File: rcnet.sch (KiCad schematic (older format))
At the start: 32 parts

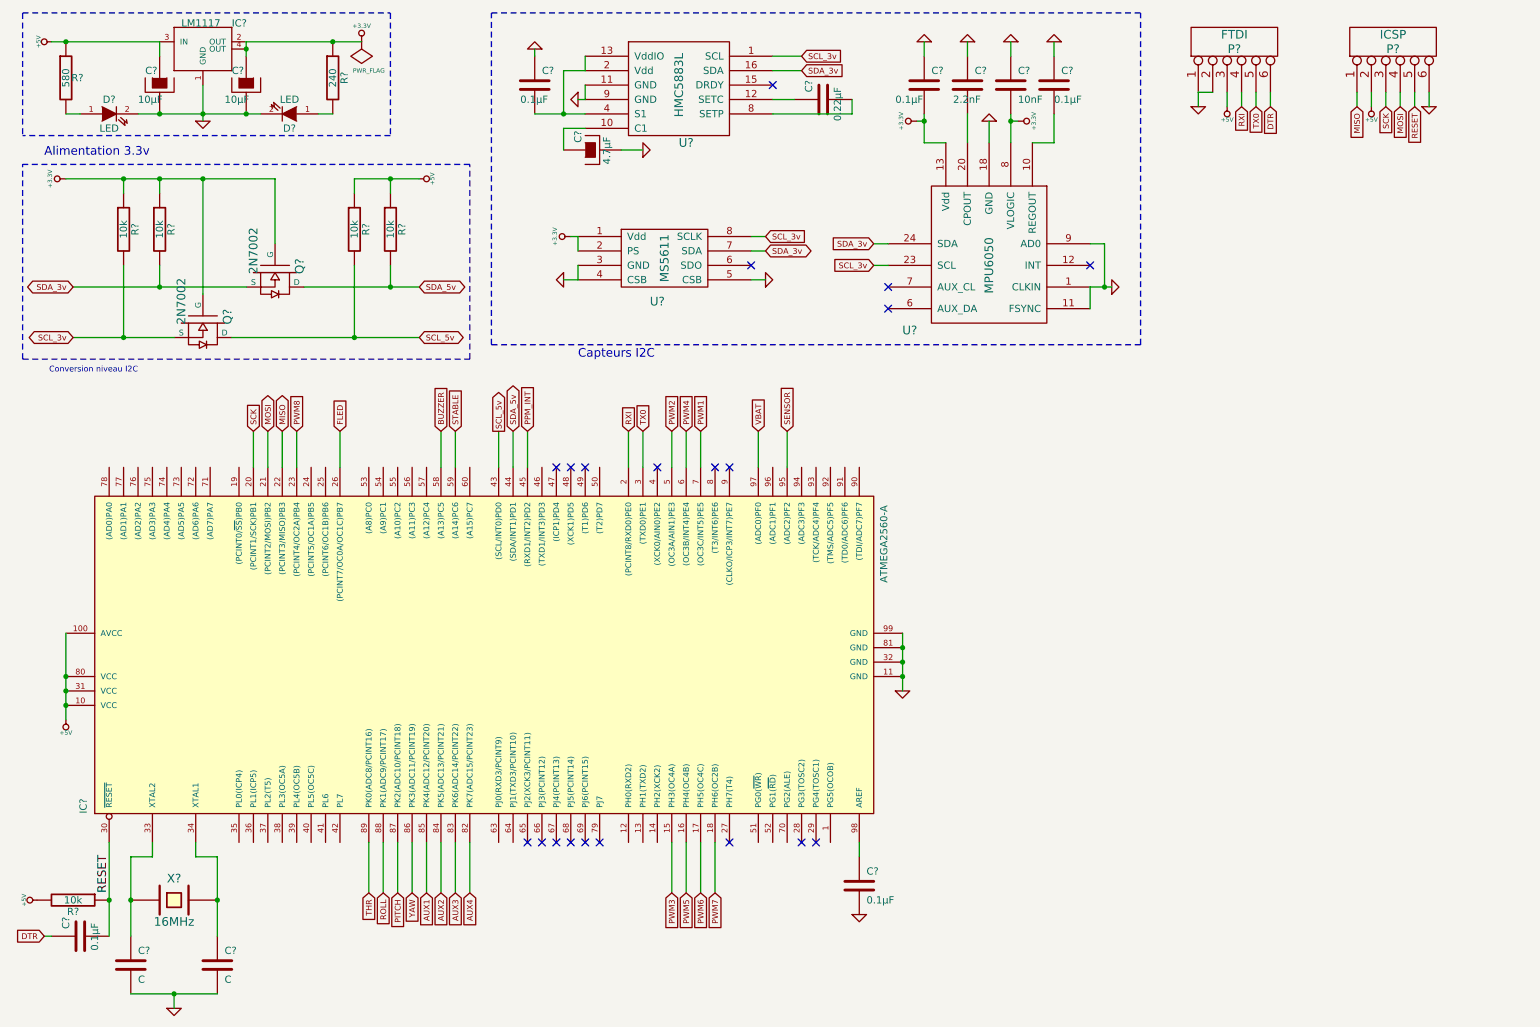
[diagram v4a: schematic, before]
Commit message: Cablage des I/O terminé, test ERC passé
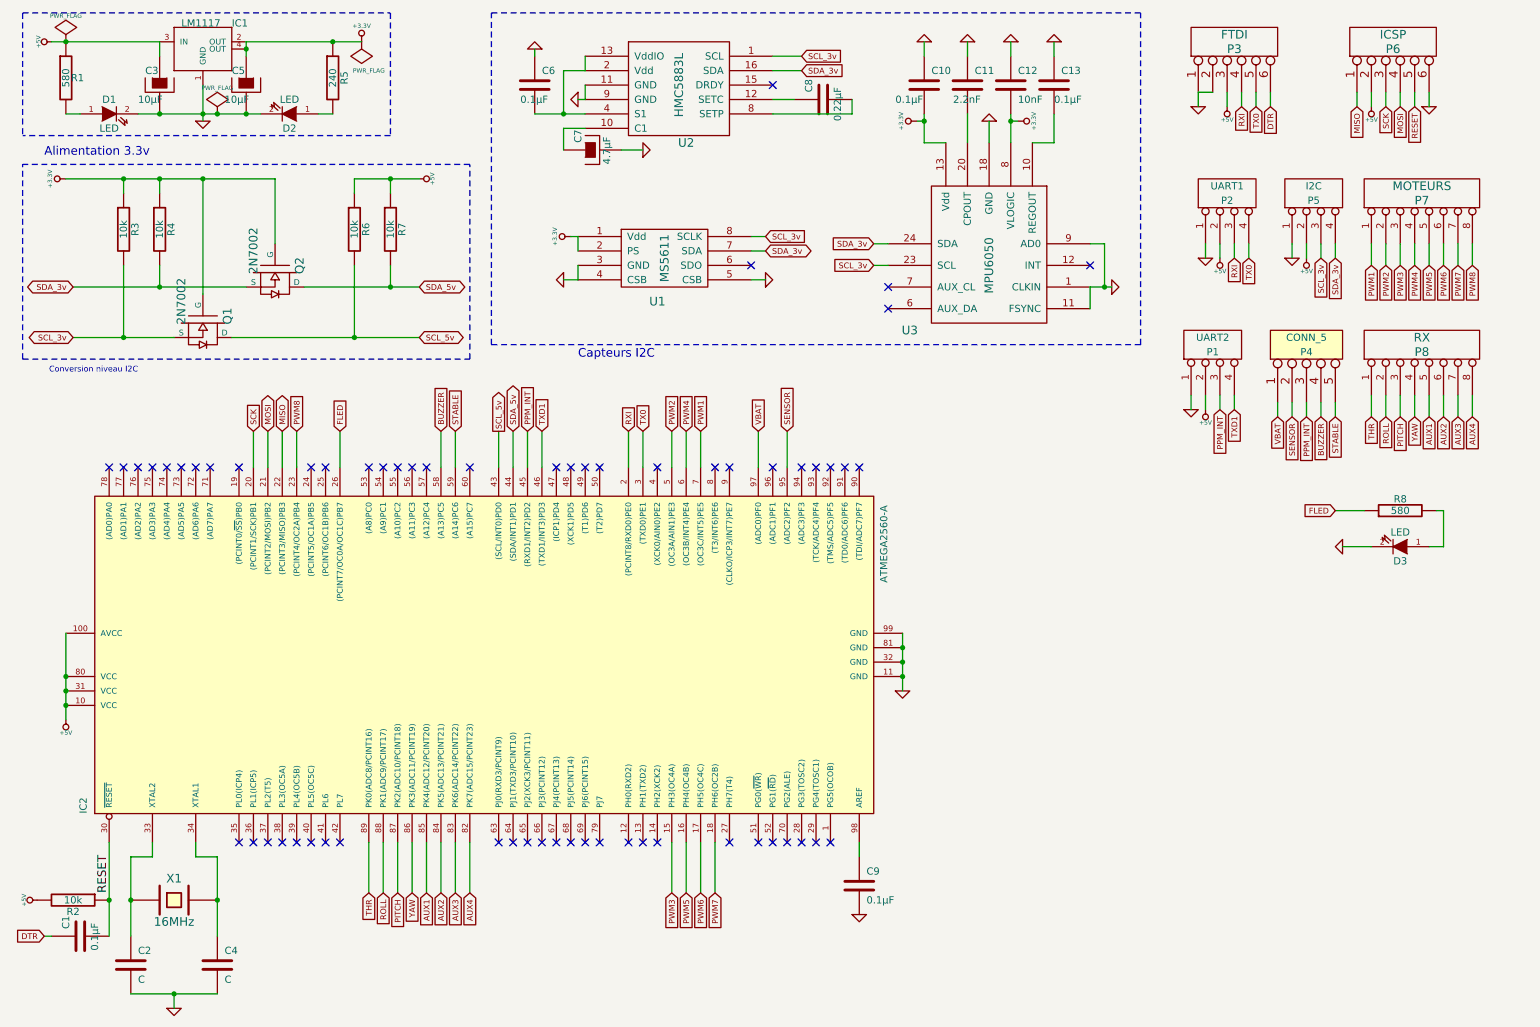
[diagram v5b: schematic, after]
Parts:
- added D3: LED, symbol LED
- added P1: UART2, symbol CONN_4
- added P2: UART1, symbol CONN_4
- added P4: CONN_5, symbol CONN_5
- added P5: I2C, symbol CONN_4
- added P7: MOTEURS, symbol CONN_8
- added P8: RX, symbol CONN_8
- added R8: 580, symbol R
- gave numbers to parts that had none: 32
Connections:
- net +5V: now also P1.2 (P2), P2.2 (P2), P5.2 (P2)
- net AUX1: now also P8.5 (P5)
- net AUX2: now also P8.6 (P6)
- net AUX3: now also P8.7 (P7)
- net AUX4: now also P8.8 (P8)
- net BUZZER: now also P4.4
- net FLED: now also R8.1
- net GND: now also D3.2 (K), P1.1 (P1), P2.1 (P1), P5.1 (P1)
- net PITCH: now also P8.3 (P3)
- net PPM_INT: now also P1.3 (P3), P4.3
- net PWM1: now also P7.1 (P1)
- net PWM2: now also P7.2 (P2)
- net PWM3: now also P7.3 (P3)
- net PWM4: now also P7.4 (P4)
- net PWM5: now also P7.5 (P5)
- net PWM6: now also P7.6 (P6)
- net PWM7: now also P7.7 (P7)
- net PWM8: now also P7.8 (P8)
- net ROLL: now also P8.2 (P2)
- net RXI: now also P2.3 (P3)
- net SCL_3v: now also P5.3 (P3)
- net SDA_3v: now also P5.4 (P4)
- net SENSOR: now also P4.2
- net STABLE: now also P4.5
- net THR: now also P8.1 (P1)
- net TX0: now also P2.4 (P4)
- net VBAT: now also P4.1
- net YAW: now also P8.4 (P4)
- net TXD1: now reaches IC2.46 ((TXD1/INT3)PD3)
- net TXD1: now also P1.4 (P4)
- new net: D3.1 (A), R8.2
- no-connect marks 20 -> 61
